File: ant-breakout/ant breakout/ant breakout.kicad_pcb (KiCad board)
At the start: 2 copper layers, 27.8 x 23.6 mm, 3 parts, among them J1 Conn_Coaxial, U1 Balun

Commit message: Updated files
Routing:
- net GND: track 5.99 -> 19.7 mm, vias 0 -> 2
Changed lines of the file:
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@@
     (thickness 1.6)
     (drawings 4)
-    (tracks 14)
+    (tracks 26)
     (zones 0)
     (modules 3)
@@
   (segment (start 120.935 94.265) (end 120.935 98.86) (width 0.25) (layer F.Cu) (net 4))
   (segment (start 120.355 93.685) (end 120.935 94.265) (width 0.25) (layer F.Cu) (net 4))
+  (segment (start 115.285 98.86) (end 120.935 98.86) (width 0.25) (layer B.Cu) (net 4))
+  (segment (start 114.36 98.86) (end 114.34 98.88) (width 0.25) (layer F.Cu) (net 4))
+  (segment (start 115.285 98.86) (end 114.36 98.86) (width 0.25) (layer F.Cu) (net 4))
+  (segment (start 114.34 98.88) (end 113.51 98.88) (width 0.25) (layer F.Cu) (net 4))
+  (segment (start 113.51 98.88) (end 113.51 98.88) (width 0.25) (layer F.Cu) (net 4))
+  (via (at 113.51 98.88) (size 0.8) (drill 0.4) (layers F.Cu B.Cu) (net 4))
+  (segment (start 120.935 98.86) (end 123.16 98.86) (width 0.25) (layer F.Cu) (net 4))
+  (segment (start 123.16 98.86) (end 123.16 98.86) (width 0.25) (layer F.Cu) (net 4))
+  (via (at 123.16 98.86) (size 0.8) (drill 0.4) (layers F.Cu B.Cu) (net 4))
+  (segment (start 123.16 98.86) (end 120.935 98.86) (width 0.25) (layer B.Cu) (net 4))
+  (segment (start 115.265 98.88) (end 115.285 98.86) (width 0.25) (layer B.Cu) (net 4))
+  (segment (start 113.51 98.88) (end 115.265 98.88) (width 0.25) (layer B.Cu) (net 4))
 )

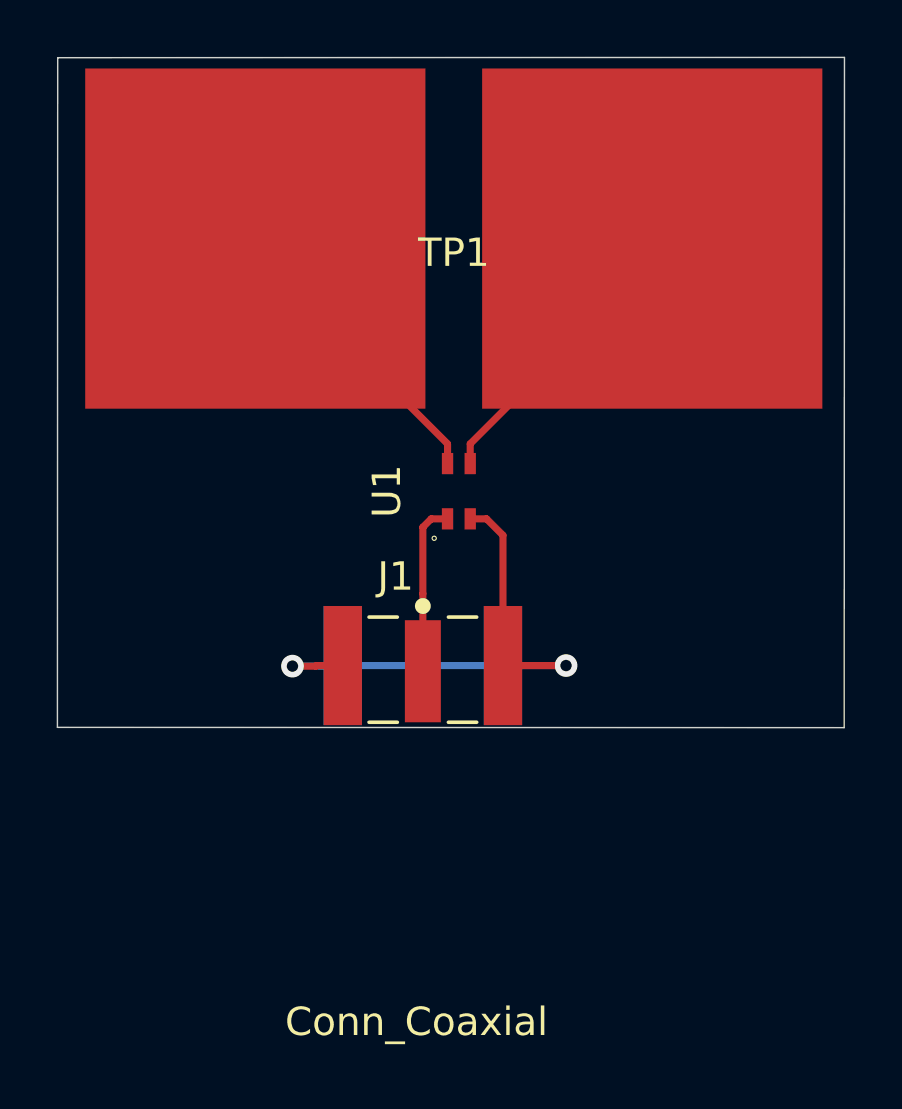
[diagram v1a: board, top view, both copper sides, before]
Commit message: updated footprint
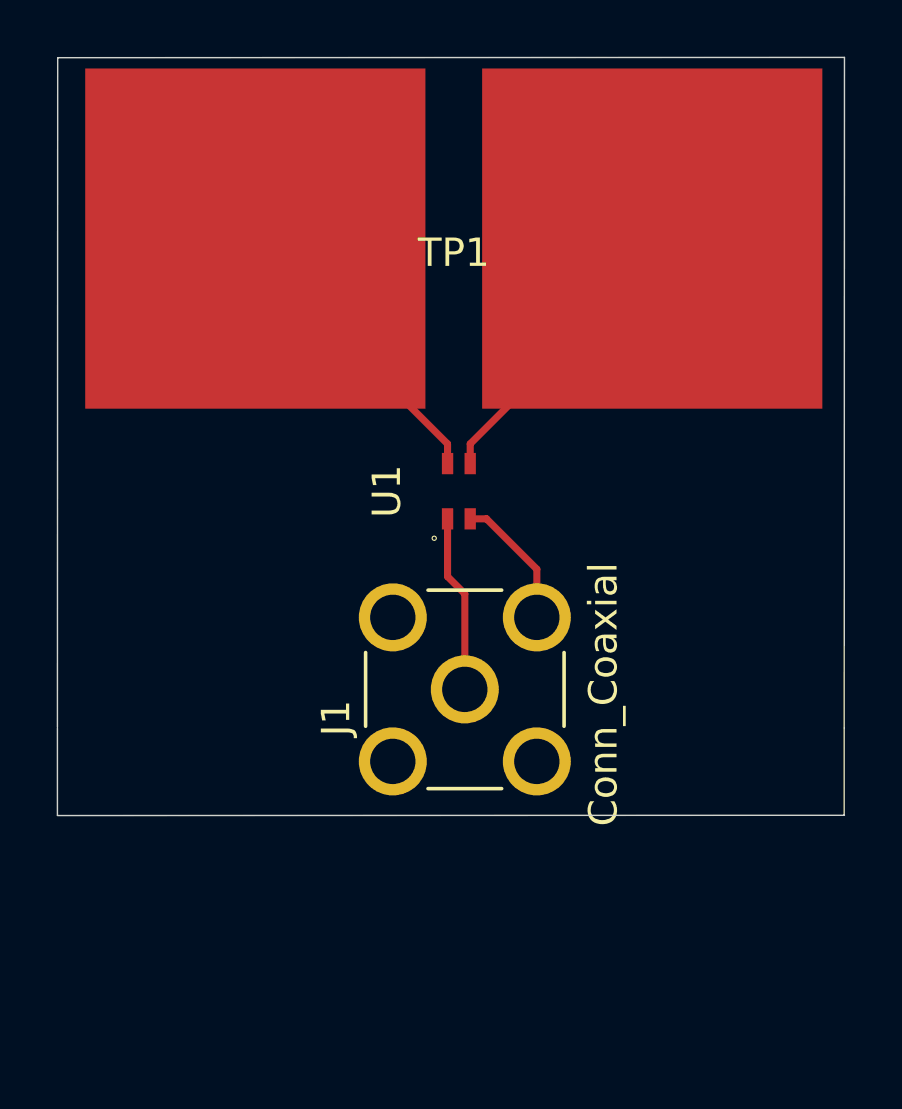
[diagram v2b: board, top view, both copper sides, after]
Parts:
- J1: footprint Documents:SMA-J-P-H-ST-EM1_N -> SMA-J-P-H-RA-TH1:SAMTEC_SMA-J-P-H-RA-TH1
- moved J1 1.61 mm to (119.6, 99.7), turned to 90 degrees
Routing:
- net GND: track 19.7 -> 4.79 mm, vias 2 -> 0
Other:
- board size 27.8 x 23.6 mm -> 27.8 x 26.7 mm
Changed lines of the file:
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@@
   (general
     (thickness 1.6)
-    (drawings 4)
-    (tracks 26)
+    (drawings 6)
+    (tracks 13)
     (zones 0)
     (modules 3)
@@
     (add_net OUT2)
   )
+  (module SMA-J-P-H-RA-TH1:SAMTEC_SMA-J-P-H-RA-TH1 (layer F.Cu)
+    (at 119.59 99.7 90)
+    (fp_text reference J1 (at -1.01137 -4.54112 90) (layer F.SilkS)
+      (effects (font (size 1.00135 1.00135) (thickness 0.05)))
+    )
+    (fp_text value Conn_Coaxial (at -0.175725 4.88518 90) (layer F.SilkS)
+      (effects (font (size 1.00415 1.00415) (thickness 0.05)))
+    )
+    (fp_line (start -3.75 3.4) (end -3.75 3.99) (layer Eco1.User) (width 0.05))
+    (fp_line (start -11.85 3.4) (end -3.75 3.4) (layer Eco1.User) (width 0.05))
+    (fp_line (start -11.85 -3.4) (end -11.85 3.4) (layer Eco1.User) (width 0.05))
+    (fp_line (start -3.75 -3.4) (end -11.85 -3.4) (layer Eco1.User) (width 0.05))
+    (fp_line (start -3.75 -3.99) (end -3.75 -3.4) (layer Eco1.User) (width 0.05))
+    (fp_line (start -11.6 3.15) (end -3.5 3.15) (layer Eco2.User) (width 0.127))
+    (fp_line (start -11.6 -3.15) (end -11.6 3.15) (layer Eco2.User) (width 0.127))
+    (fp_line (start -3.5 -3.15) (end -11.6 -3.15) (layer Eco2.User) (width 0.127))
+    (fp_line (start 3.99 3.99) (end -3.75 3.99) (layer Eco1.User) (width 0.05))
+    (fp_line (start 3.99 -3.99) (end 3.99 3.99) (layer Eco1.User) (width 0.05))
+    (fp_line (start -3.75 -3.99) (end 3.99 -3.99) (layer Eco1.User) (width 0.05))
+    (fp_line (start 1.3 3.5) (end -1.3 3.5) (layer F.SilkS) (width 0.127))
+    (fp_line (start -3.5 1.3) (end -3.5 -1.3) (layer F.SilkS) (width 0.127))
+    (fp_line (start 3.5 1.3) (end 3.5 -1.3) (layer F.SilkS) (width 0.127))
+    (fp_line (start -1.3 -3.5) (end 1.3 -3.5) (layer F.SilkS) (width 0.127))
+    (fp_line (start -3.5 -3.15) (end -3.5 -3.5) (layer Eco2.User) (width 0.127))
+    (fp_line (start -3.5 3.15) (end -3.5 -3.15) (layer Eco2.User) (width 0.127))
+    (fp_line (start -3.5 3.5) (end -3.5 3.15) (layer Eco2.User) (width 0.127))
+    (fp_line (start 3.5 3.5) (end -3.5 3.5) (layer Eco2.User) (width 0.127))
+    (fp_line (start 3.5 -3.5) (end 3.5 3.5) (layer Eco2.User) (width 0.127))
+    (fp_line (start -3.5 -3.5) (end 3.5 -3.5) (layer Eco2.User) (width 0.127))
+    (pad 5 thru_hole circle (at -2.54 2.54 90) (size 2.4 2.4) (drill 1.6) (layers *.Cu *.Mask))
+    (pad 2 thru_hole circle (at 2.54 2.54 90) (size 2.4 2.4) (drill 1.6) (layers *.Cu *.Mask)
+      (net 4 GND))
+    (pad 3 thru_hole circle (at 2.54 -2.54 90) (size 2.4 2.4) (drill 1.6) (layers *.Cu *.Mask))
+    (pad 4 thru_hole circle (at -2.54 -2.54 90) (size 2.4 2.4) (drill 1.6) (layers *.Cu *.Mask))
+    (pad 1 thru_hole circle (at 0 0 90) (size 2.4 2.4) (drill 1.6) (layers *.Cu *.Mask)
+      (net 1 "Net-(J1-Pad1)"))
+  )
   (module "Documents:exposed pad" (layer F.Cu)
     (at 119.2 83.8)
@@
     (pad 2 smd rect (at 7 0) (size 12 12) (layers F.Cu F.Paste F.Mask)
       (net 2 OUT2))
-  )
-  (module Documents:SMA-J-P-H-ST-EM1_N (layer F.Cu)
-    (at 118.11 99.06)
-    (attr smd)
-    (fp_text reference J1 (at -0.96165 -3.34077) (layer F.SilkS)
-      (effects (font (size 1.00173 1.00173) (thickness 0.05)))
-    )
-    (fp_text value Conn_Coaxial (at -0.22506 12.3676) (layer F.SilkS)
-      (effects (font (size 1.0002 1.0002) (thickness 0.05)))
-    )
-    (fp_line (start 3.175 1.9) (end 3.165 11.42) (layer Eco2.User) (width 0.127))
-    (fp_line (start 3.165 11.42) (end -3.165 11.42) (layer Eco2.User) (width 0.127))
-    (fp_line (start -3.165 11.42) (end -3.175 1.9) (layer Eco2.User) (width 0.127))
-    (fp_line (start -5 1.9) (end -3.175 1.9) (layer Eco2.User) (width 0.127))
-    (fp_line (start -3.175 1.9) (end 3.175 1.9) (layer Eco2.User) (width 0.127))
-    (fp_line (start 3.175 1.9) (end 5 1.9) (layer Eco2.User) (width 0.127))
-    (fp_line (start -3.175 1.9) (end -3.175 -1.91) (layer Eco2.User) (width 0.127))
-    (fp_line (start -3.175 -1.91) (end 3.175 -1.91) (layer Eco2.User) (width 0.127))
-    (fp_line (start 3.175 -1.91) (end 3.175 1.9) (layer Eco2.User) (width 0.127))
-    (fp_line (start -1.9 1.8) (end -0.9 1.8) (layer F.SilkS) (width 0.127))
-    (fp_line (start 0.9 1.8) (end 1.9 1.8) (layer F.SilkS) (width 0.127))
-    (fp_line (start -1.9 -1.91) (end -0.9 -1.91) (layer F.SilkS) (width 0.127))
-    (fp_line (start 0.9 -1.91) (end 1.9 -1.91) (layer F.SilkS) (width 0.127))
-    (fp_circle (center 0 -2.3) (end 0.14 -2.3) (layer F.SilkS) (width 0.28))
-    (fp_line (start -3.75 -2.55) (end 3.75 -2.55) (layer Eco1.User) (width 0.05))
-    (fp_line (start 3.75 -2.55) (end 3.75 2.15) (layer Eco1.User) (width 0.05))
-    (fp_line (start 3.75 2.15) (end 3.425 2.15) (layer Eco1.User) (width 0.05))
-    (fp_line (start 3.425 2.15) (end 3.425 11.67) (layer Eco1.User) (width 0.05))
-    (fp_line (start 3.425 11.67) (end -3.425 11.67) (layer Eco1.User) (width 0.05))
-    (fp_line (start -3.425 11.67) (end -3.425 2.15) (layer Eco1.User) (width 0.05))
-    (fp_line (start -3.425 2.15) (end -3.75 2.15) (layer Eco1.User) (width 0.05))
-    (fp_line (start -3.75 2.15) (end -3.75 -2.55) (layer Eco1.User) (width 0.05))
-    (pad 1 smd rect (at 0 0) (size 1.27 3.6) (layers F.Cu F.Paste F.Mask)
-      (net 1 "Net-(J1-Pad1)"))
-    (pad 2 smd rect (at -2.825 -0.2) (size 1.35 4.2) (layers F.Cu F.Paste F.Mask)
-      (net 4 GND))
-    (pad 2 smd rect (at 2.825 -0.2) (size 1.35 4.2) (layers F.Cu F.Paste F.Mask)
-      (net 4 GND))
-    (pad 2 smd rect (at -2.825 -0.2) (size 1.35 4.2) (layers B.Cu F.Paste F.Mask)
-      (net 4 GND))
-    (pad 2 smd rect (at 2.825 -0.2) (size 1.35 4.2) (layers B.Cu F.Paste F.Mask)
-      (net 4 GND))
   )
   (module Documents:Balun (layer F.Cu)
@@
       (net 4 GND))
   )
+  (gr_line (start 132.97 101.07) (end 132.97 104.13) (layer Edge.Cuts) (width 0.05))
+  (gr_line (start 105.22 101.07) (end 105.22 104.14) (layer Edge.Cuts) (width 0.05))
   (gr_line (start 105.23 77.42) (end 105.22 101.04) (layer Edge.Cuts) (width 0.05))
   (gr_line (start 132.98 77.41) (end 105.23 77.42) (layer Edge.Cuts) (width 0.05))
   (gr_line (start 132.97 101.05) (end 132.98 77.41) (layer Edge.Cuts) (width 0.05))
-  (gr_line (start 105.22 101.04) (end 132.97 101.05) (layer Edge.Cuts) (width 0.05))
-  (segment (start 118.11 96.324233) (end 118.11 99.06) (width 0.25) (layer F.Cu) (net 1))
-  (segment (start 118.11 93.98) (end 118.11 96.324233) (width 0.25) (layer F.Cu) (net 1))
-  (segment (start 118.405 93.685) (end 118.11 93.98) (width 0.25) (layer F.Cu) (net 1))
-  (segment (start 118.98 93.685) (end 118.405 93.685) (width 0.25) (layer F.Cu) (net 1))
+  (gr_line (start 105.22 104.15) (end 132.98 104.14) (layer Edge.Cuts) (width 0.05))
+  (segment (start 119.59 99.7) (end 119.59 96.33) (width 0.25) (layer F.Cu) (net 1))
+  (segment (start 118.98 95.72) (end 118.98 93.685) (width 0.25) (layer F.Cu) (net 1))
+  (segment (start 119.59 96.33) (end 118.98 95.72) (width 0.25) (layer F.Cu) (net 1))
   (segment (start 119.78 91.735) (end 119.78 91.04) (width 0.25) (layer F.Cu) (net 2))
   (segment (start 119.78 91.04) (end 121.92 88.9) (width 0.25) (layer F.Cu) (net 2))
@@
   (segment (start 118.98 91.04) (end 116.84 88.9) (width 0.25) (layer F.Cu) (net 3))
   (segment (start 116.84 88.9) (end 116.84 88.9) (width 0.25) (layer F.Cu) (net 3))
+  (segment (start 122.13 95.46) (end 122.13 97.16) (width 0.25) (layer F.Cu) (net 4))
+  (segment (start 120.355 93.685) (end 122.13 95.46) (width 0.25) (layer F.Cu) (net 4))
   (segment (start 119.78 93.685) (end 120.355 93.685) (width 0.25) (layer F.Cu) (net 4))
-  (segment (start 120.935 94.265) (end 120.935 98.86) (width 0.25) (layer F.Cu) (net 4))
-  (segment (start 120.355 93.685) (end 120.935 94.265) (width 0.25) (layer F.Cu) (net 4))
-  (segment (start 115.285 98.86) (end 120.935 98.86) (width 0.25) (layer B.Cu) (net 4))
-  (segment (start 114.36 98.86) (end 114.34 98.88) (width 0.25) (layer F.Cu) (net 4))
-  (segment (start 115.285 98.86) (end 114.36 98.86) (width 0.25) (layer F.Cu) (net 4))
-  (segment (start 114.34 98.88) (end 113.51 98.88) (width 0.25) (layer F.Cu) (net 4))
-  (segment (start 113.51 98.88) (end 113.51 98.88) (width 0.25) (layer F.Cu) (net 4))
-  (via (at 113.51 98.88) (size 0.8) (drill 0.4) (layers F.Cu B.Cu) (net 4))
-  (segment (start 120.935 98.86) (end 123.16 98.86) (width 0.25) (layer F.Cu) (net 4))
-  (segment (start 123.16 98.86) (end 123.16 98.86) (width 0.25) (layer F.Cu) (net 4))
-  (via (at 123.16 98.86) (size 0.8) (drill 0.4) (layers F.Cu B.Cu) (net 4))
-  (segment (start 123.16 98.86) (end 120.935 98.86) (width 0.25) (layer B.Cu) (net 4))
-  (segment (start 115.265 98.88) (end 115.285 98.86) (width 0.25) (layer B.Cu) (net 4))
-  (segment (start 113.51 98.88) (end 115.265 98.88) (width 0.25) (layer B.Cu) (net 4))
 )
